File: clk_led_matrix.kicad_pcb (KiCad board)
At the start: 2 copper layers, 89.7 x 33.2 mm, 50 parts, among them J1 USB_C_Receptacle_USB2.0_16P, J10 LED_MATRIX_0, J2 LED_MATRIX_0, J3 CH32_prog, J4 STM32_prog, J5 Conn_Coaxial, J6 LED_MATRIX_0, J7 LED_MATRIX_0, J8 LED_MATRIX_0, J9 LED_MATRIX_0, SW1 RST, SW2 BOOT, U1 STM32C071KBUx, U2 AMS1117-3.3, U3 ATGM336H-5N31, Y1 Q13FC13500004

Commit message: update layout and usb c connector
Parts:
- removed R3: 0, Resistor_SMD:R_0603_1608Metric
- added D4: LED_CLK, LED_SMD:LED_0805_2012Metric, F.Cu at (88.9, 88.3)
- added D5: LED_CLK, LED_SMD:LED_0805_2012Metric, F.Cu at (92.6, 93.3)
- added D6: LED_CLK, LED_SMD:LED_0805_2012Metric, F.Cu at (99.1, 95.7)
- added D7: LED_CLK, LED_SMD:LED_0805_2012Metric, F.Cu at (92.4, 98.6)
- added H1: MountingHole_Pad, MountingHole:MountingHole_3.2mm_M3_Pad_Via, F.Cu at (103.3, 109.6)
- added H2: MountingHole_Pad, MountingHole:MountingHole_3.2mm_M3_Pad_Via, F.Cu at (186.0, 109.6)
- added H3: MountingHole_Pad, MountingHole:MountingHole_3.2mm_M3_Pad_Via, F.Cu at (186.0, 135.8)
- added H4: MountingHole_Pad, MountingHole:MountingHole_3.2mm_M3_Pad_Via, F.Cu at (103.3, 135.8)
- added R20: 5k1, Resistor_SMD:R_0603_1608Metric, F.Cu at (88.9, 86.5)
- added R21: 5k1, Resistor_SMD:R_0603_1608Metric, F.Cu at (92.6, 91.5)
- added R22: 5k1, Resistor_SMD:R_0603_1608Metric, F.Cu at (99.1, 93.9)
- added R23: 5k1, Resistor_SMD:R_0603_1608Metric, F.Cu at (92.4, 96.8)
- J1: footprint Connector_USB:USB_C_Receptacle_GCT_USB4115-03-C -> easyeda2kicad:USB-C-TH_SHOUHAN_TYPE-C-14PLC-H10.0
- moved C4 97.1 mm to (163.4, 133.0)
- moved U2 87.9 mm to (156.9, 133.1)
- moved C3 83.3 mm to (151.0, 135.8), turned to -90 degrees
- moved J3 59.8 mm to (117.1, 108.5), turned to -90 degrees
- moved D2 50.7 mm to (130.7, 96.2)
- moved R11 50.7 mm to (130.7, 94.3)
- moved J4 45.2 mm to (127.0, 108.5), turned to -90 degrees
- moved C7 45.0 mm to (118.8, 134.0)
- moved R15 45.0 mm to (115.8, 134.0)
- moved SW1 45.0 mm to (117.3, 136.7)
- moved TP2 45.0 mm to (121.6, 136.7)
- moved R13 39.8 mm to (129.2, 134.1)
- moved R14 39.8 mm to (126.2, 134.1)
- moved SW2 39.8 mm to (127.7, 136.7)
- moved C2 35.8 mm to (138.4, 109.7), turned to 90 degrees
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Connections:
- J1 pad SH: Net-(J1-SHIELD) -> GND
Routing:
- net /SCL_CH32: track 133.6 -> 89.7 mm
- net /SDA_CH32: track 117.1 -> 82.7 mm
- net Net-(U1-PB7): track 31.1 -> 0.00 mm
- net +3V3: track 0.00 -> 22.5 mm, vias 0 -> 16
- net /USB_N: track 0.00 -> 16.3 mm, vias 0 -> 1
- net /USB_P: track 0.00 -> 16.3 mm, vias 0 -> 1
- net /XIN: track 0.00 -> 7.43 mm
- net /XOUT: track 0.00 -> 7.31 mm
- net VBUS: track 0.00 -> 5.66 mm, vias 0 -> 1
- net Net-(J1-CC2): track 0.00 -> 4.49 mm
- net +5V: track 0.00 -> 4.28 mm
- net /VCC_RF: track 0.00 -> 3.72 mm
- net Net-(U1-PA7): track 3.69 -> 0.00 mm
- net Net-(U1-PB9): track 3.43 -> 0.00 mm
- net /GNSS_UART_FROM_MODULE_TO_STM32: track 0.00 -> 3.29 mm
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- added copper zone on F.Cu, net +3V3
- added copper zone on In2.Cu, net +3V3
- added copper zone on B.Cu, net GND
- added copper zone on F.Cu, net GND
- added copper zone on In1.Cu, net GND
- added copper zone on In2.Cu, net VBUS
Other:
- copper layers 2 -> 4

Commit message: Update layout
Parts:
- moved J5 82.3 mm to (103.6, 116.8), turned to 90 degrees
- moved L1 65.9 mm to (108.5, 112.9), turned to 90 degrees
- moved U3 51.6 mm to (115.6, 115.4), turned to -90 degrees
- moved J3 51.5 mm to (168.6, 108.6)
- moved R10 35.7 mm to (124.2, 119.5), turned to 180 degrees
- moved R9 35.0 mm to (124.2, 118.0), turned to 180 degrees
- moved C6 34.8 mm to (124.2, 112.1), turned to 0 degrees
- moved R8 34.6 mm to (124.2, 116.5), turned to 180 degrees
- moved C5 34.4 mm to (124.2, 114.3), turned to 0 degrees
- moved J4 33.7 mm to (160.7, 108.6)
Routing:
- net VBUS: track 5.66 -> 0.00 mm, vias 1 -> 2
- added copper zone on F.Cu, net VBUS

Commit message: finished layout
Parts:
- TP1: moved to B.Cu
- moved R23 73.9 mm to (161.7, 122.4), turned to 90 degrees
- moved D7 70.6 mm to (159.0, 122.0)
- moved R22 70.0 mm to (161.7, 125.3), turned to -90 degrees
- moved D6 66.9 mm to (159.0, 125.6)
- moved R11 58.2 mm to (170.2, 137.0), turned to 90 degrees
- moved D2 58.1 mm to (172.1, 137.0), turned to 90 degrees
- moved R20 57.4 mm to (133.7, 122.4), turned to 90 degrees
- moved D4 53.7 mm to (130.7, 122.0)
- moved R21 53.3 mm to (133.7, 125.4), turned to -90 degrees
- moved D3 52.2 mm to (166.5, 137.0), turned to 90 degrees
- moved R12 50.6 mm to (164.7, 137.0), turned to -90 degrees
- moved D5 49.9 mm to (130.7, 125.6)
- moved TP1 2.89 mm to (139.0, 116.2)
- moved J5 2.88 mm to (106.0, 118.4), turned to 180 degrees
- moved R1 1.92 mm to (147.0, 129.6)
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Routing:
- net Net-(D3-A): track 0.00 -> 106.7 mm, vias 0 -> 2
- net /STM32_SWCLK: track 0.00 -> 99.1 mm, vias 0 -> 2
- net /SWDIO_ch32: track 0.00 -> 90.5 mm
- net /NRST: track 2.72 -> 72.2 mm, vias 1 -> 2
- net /SDA_CH32: track 82.7 -> 133.5 mm
- net /SCL_CH32: track 89.7 -> 121.8 mm, vias 5 -> 2
- net /GNSS_I2C_SDA: track 0.00 -> 30.3 mm
- net /GNSS_I2C_SCL: track 0.00 -> 27.2 mm
- net Net-(U1-PB7): track 0.00 -> 25.3 mm, vias 0 -> 2
- net /STM32_SWIO: track 0.00 -> 22.9 mm, vias 0 -> 1
- net Net-(U1-PA0): track 0.00 -> 20.8 mm
- net Net-(U1-PA1): track 0.00 -> 20.2 mm
- net /RF_IN: track 0.00 -> 8.81 mm
- net +3V3: track 22.5 -> 30.7 mm, vias 16 -> 19
- net Net-(R15-Pad2): track 0.00 -> 4.12 mm
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
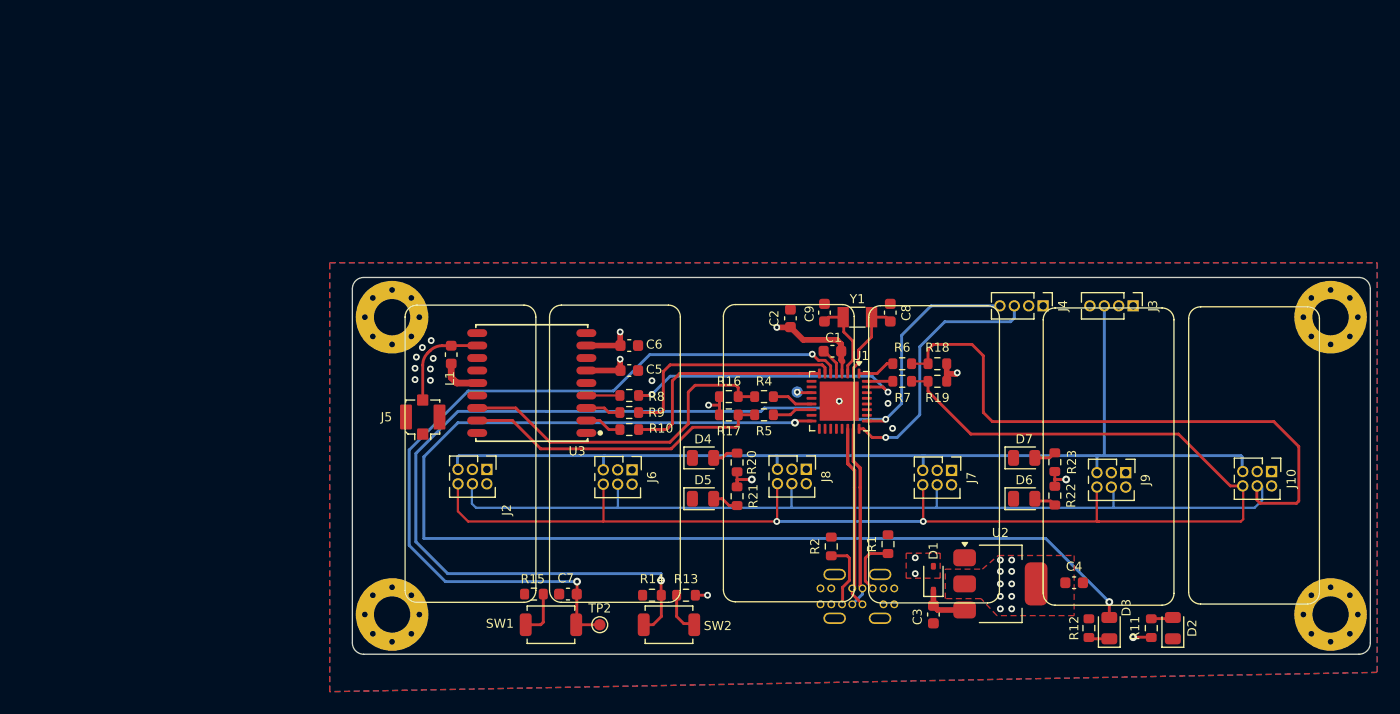
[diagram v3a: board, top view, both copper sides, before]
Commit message: update schematic and layout
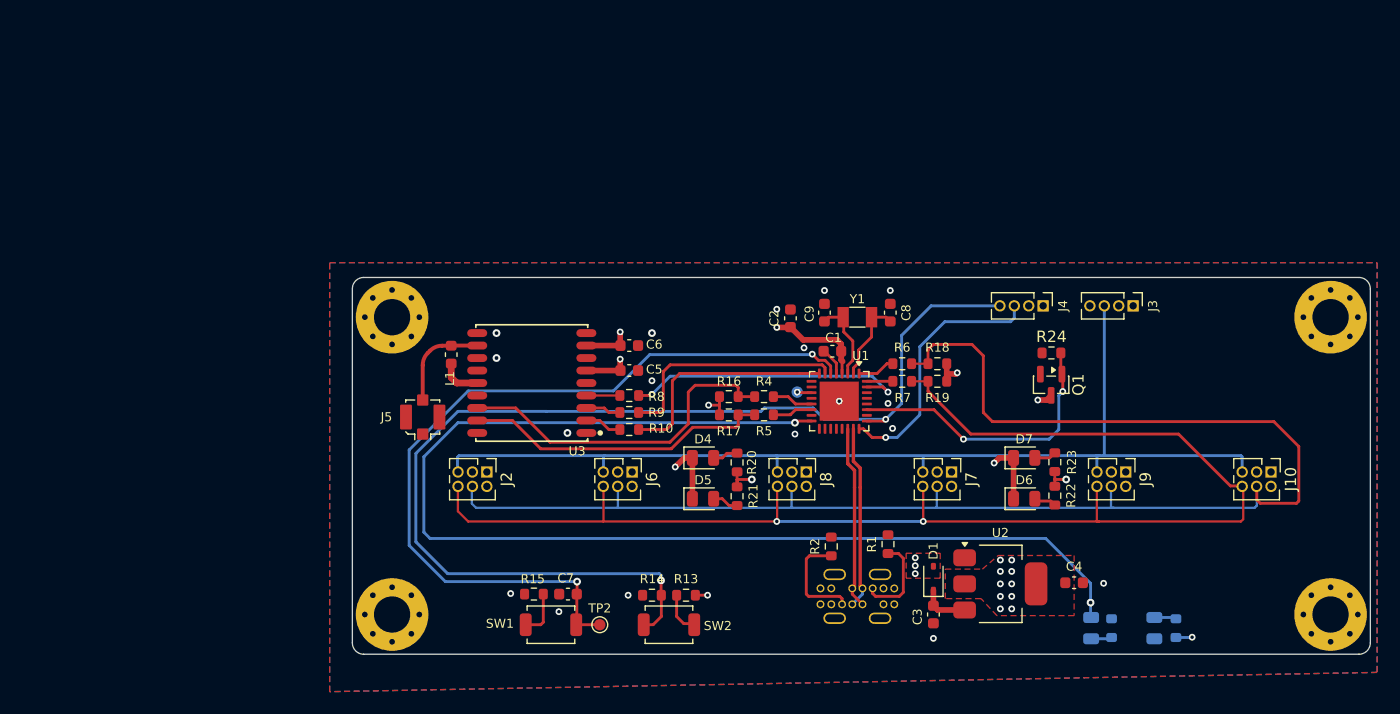
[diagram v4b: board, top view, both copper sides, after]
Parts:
- added Q1: 2N7002, Package_TO_SOT_SMD:SOT-23, F.Cu at (161.4, 115.6)
- added R24: 5k1, Resistor_SMD:R_0603_1608Metric, F.Cu at (161.4, 112.8)
- D2, D3, R11, R12: moved to B.Cu
- R20, R21, R22, R23: value 5k1 -> 100
- moved J2 2.71 mm to (111.7, 123.2)
- moved R11 2.17 mm to (172.4, 137.0)
- moved R12 2.00 mm to (166.7, 137.0)
- moved D2 1.63 mm to (170.5, 137.0)
- moved D3 1.60 mm to (164.9, 137.0)
- moved J8 0.24 mm to (139.8, 123.2)
- moved J6 0.19 mm to (124.5, 123.2)
- moved J7 0.14 mm to (152.6, 123.2)
- moved J10 0.06 mm to (180.8, 123.2)
- moved J9 0.06 mm to (167.9, 123.2)
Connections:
- D4 pad 1: GND -> Net-(D4-K)
- D5 pad 1: GND -> Net-(D4-K)
- D6 pad 1: GND -> Net-(D4-K)
- D7 pad 1: GND -> Net-(D4-K)
- U1 pad 27: unconnected-(U1-PB3-Pad27) -> /LED_DRIVE
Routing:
- net Net-(D4-K): track 0.00 -> 48.3 mm, vias 0 -> 3
- net /LED_DRIVE: track 0.00 -> 25.3 mm, vias 0 -> 2
- net GND: track 2.47 -> 11.8 mm, vias 12 -> 18
- net Net-(J1-CC2): track 6.03 -> 9.23 mm
- net Net-(J1-CC1): track 5.25 -> 7.92 mm
- net Net-(D3-A): track 106.7 -> 105.8 mm
- net VBUS: vias 2 -> 3
